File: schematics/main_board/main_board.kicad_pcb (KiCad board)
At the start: 2 copper layers, 184.9 x 184.9 mm, 56 parts, among them J1 USB_B_Micro, M1 Motor_DC, M2 Motor_DC, M3 Motor_DC, M4 Motor_DC, Q1 BC817, Q2 2N7002, Q3 2N7002, Q4 2N7002, Q5 2N7002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

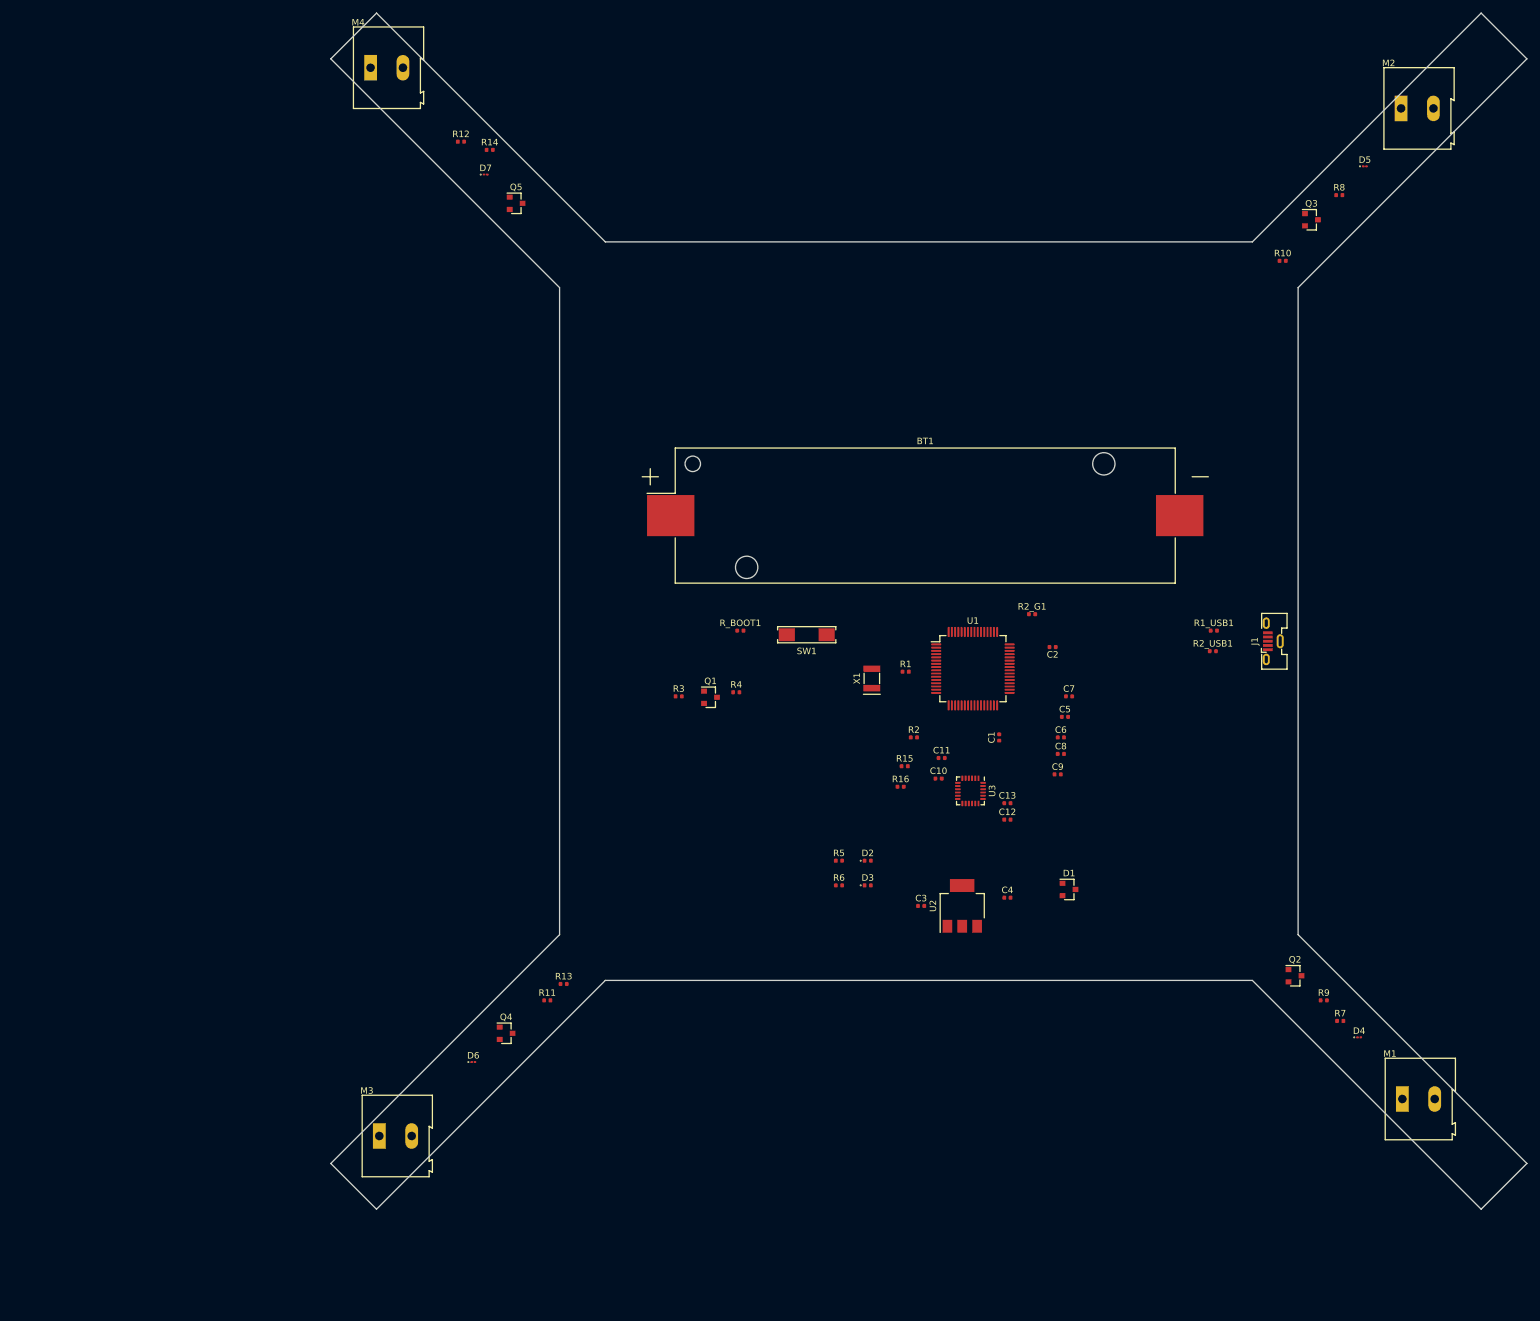
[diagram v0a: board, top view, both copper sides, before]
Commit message: Changed some footprints, added some traces
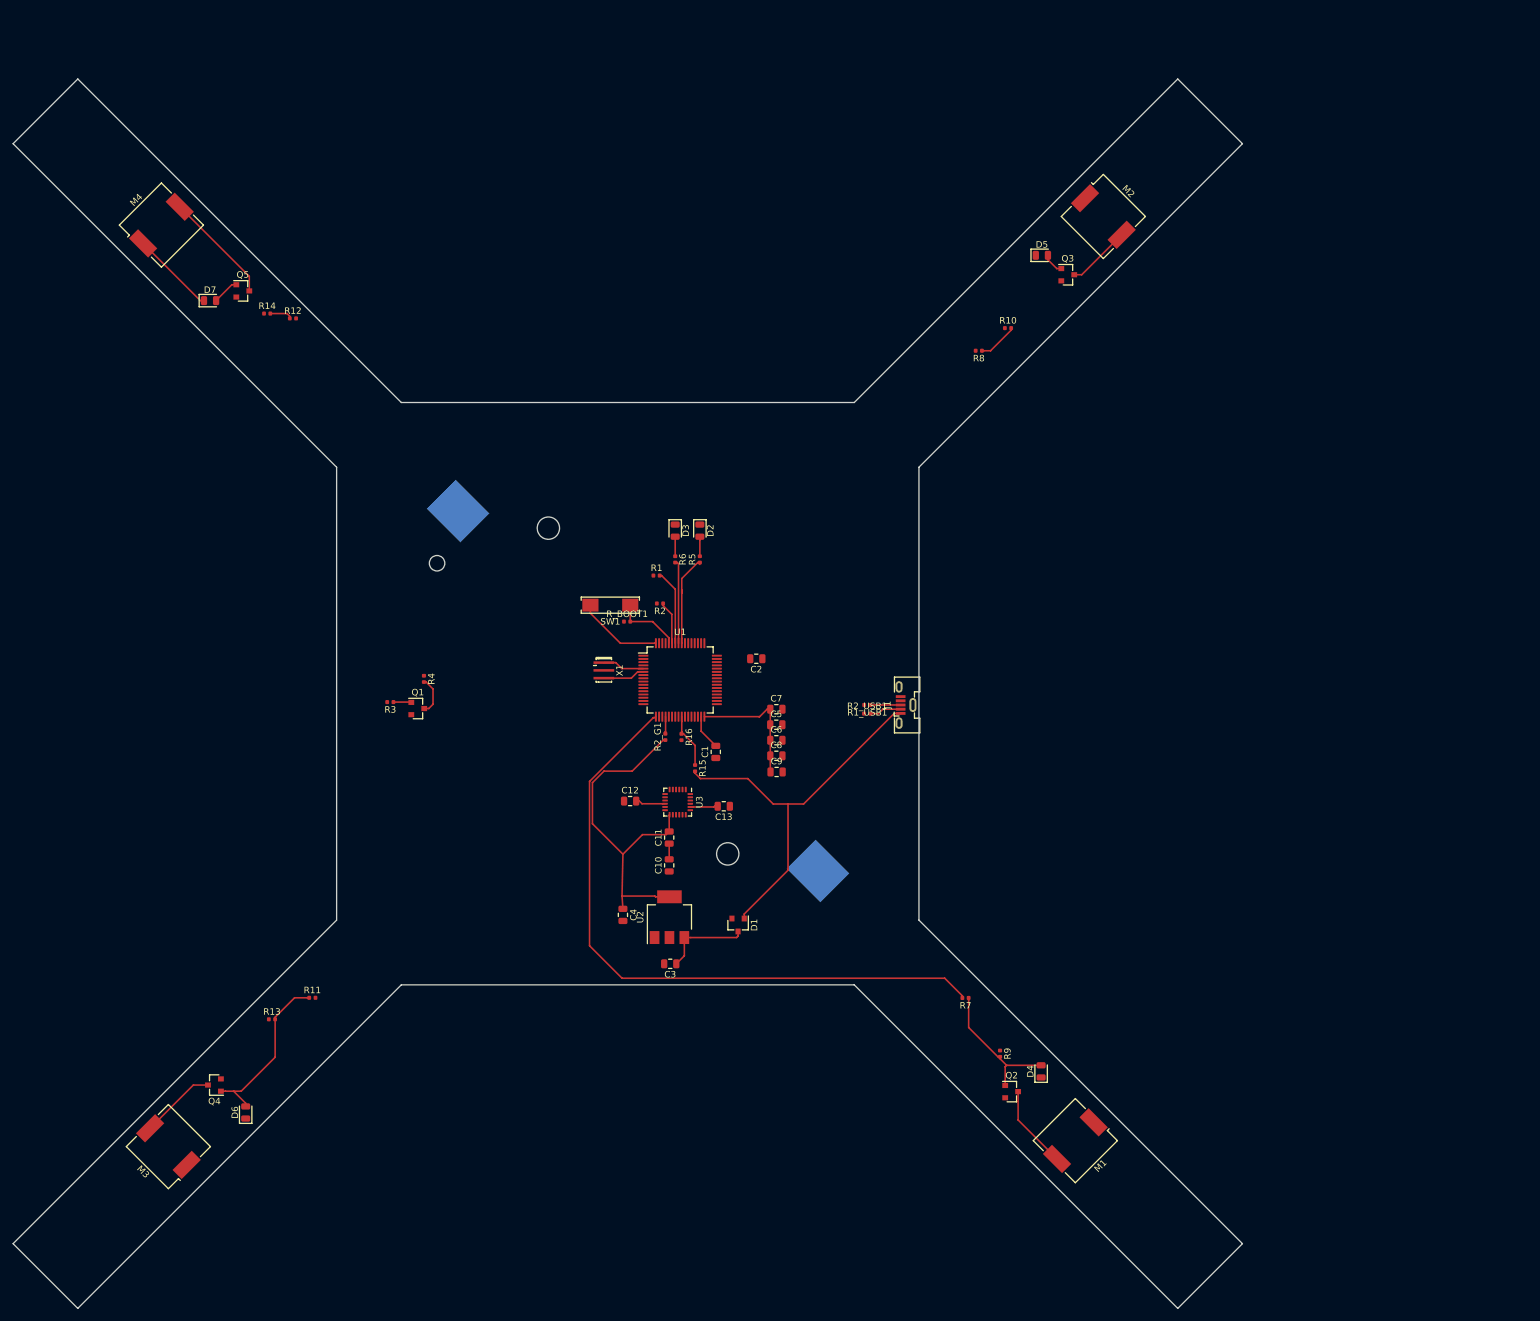
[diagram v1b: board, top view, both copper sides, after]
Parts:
- BT1: moved to B.Cu
- C1, C10, C11, C12, C13, C2, C3, C4, C5, C6, C7, C8, C9: footprint Capacitor_SMD:C_0402_1005Metric -> Capacitor_SMD:C_0805_2012Metric
- D2, D3: footprint LED_SMD:LED_0402_1005Metric -> LED_SMD:LED_0805_2012Metric
- D4, D5, D6, D7: footprint Diode_SMD:D_01005_0402Metric -> Diode_SMD:D_0805_2012Metric
- M1, M2, M3, M4: footprint TerminalBlock:TerminalBlock_Altech_AK300-2_P5.00mm -> Buzzer_Beeper:Buzzer_CUI_CPT-9019S-SMT
- X1: footprint Crystal:Resonator_SMD_muRata_CDSCB-2Pin_4.5x2.0mm -> Crystal:Resonator_SMD_muRata_CSTxExxV-3Pin_3.0x1.1mm_HandSoldering
- moved D3 62.4 mm to (142.3, 119.8), turned to 270 degrees
- moved R8 60.7 mm to (189.2, 92.0), turned to 180 degrees
- moved R2_G1 59.8 mm to (140.8, 151.7), turned to 90 degrees
- moved C4 59.5 mm to (134.2, 179.2), turned to 270 degrees
- moved C12 58.4 mm to (135.4, 161.6)
- moved R7 58.0 mm to (187.2, 192.0), turned to 180 degrees
- moved J1 57.6 mm to (178.0, 146.8)
- moved D2 57.2 mm to (146.1, 119.8), turned to 270 degrees
- moved R6 56.4 mm to (142.3, 124.2), turned to 270 degrees
- moved R1_USB1 54.8 mm to (172.0, 146.7), turned to 180 degrees
- moved R2_USB1 54.3 mm to (172.0, 148.1)
- moved BT1 52.0 mm to (136.6, 144.6), turned to 315 degrees
- moved D5 51.8 mm to (199.0, 77.2)
- moved D1 51.4 mm to (152.1, 180.8), turned to 270 degrees
- moved R5 51.3 mm to (146.1, 124.2), turned to 90 degrees
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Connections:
- BT1 pad 1: VBAT_PAD -> BAT+
- D1 pad 2: 5V_EXTERNAL -> BAT+
- D4 pad 1: VBAT_PAD -> BAT+
- D5 pad 1: VBAT_PAD -> BAT+
- D6 pad 1: VBAT_PAD -> BAT+
- D7 pad 1: VBAT_PAD -> BAT+
- M1 pad 1: VBAT_PAD -> BAT+
- M2 pad 1: VBAT_PAD -> BAT+
- M3 pad 1: VBAT_PAD -> BAT+
- M4 pad 1: VBAT_PAD -> BAT+
- R4 pad 1: 5V_EXTERNAL -> BAT+
- U1 pad 16: M4 -> S4
- U1 pad 17: M1 -> S1
- U1 pad 9: VBAT_PAD -> BAT+
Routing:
- net S1: track 0.00 -> 100.9 mm
- net VCC: track 0.00 -> 87.7 mm
- net 5V_USB: track 0.00 -> 60.3 mm
- net Net-(D6-Pad2): track 0.00 -> 26.4 mm
- net Net-(D4-Pad2): track 0.00 -> 21.6 mm
- net Net-(M4-Pad2): track 0.00 -> 17.5 mm
- net LED1: track 0.00 -> 14.7 mm
- net Net-(C3-Pad1): track 0.00 -> 13.7 mm
- net BAT+: track 0.00 -> 13.1 mm
- net Net-(M1-Pad2): track 0.00 -> 12.9 mm
- net LED2: track 0.00 -> 12.9 mm
- net Net-(M3-Pad2): track 0.00 -> 11.7 mm
- net Net-(R1-Pad2): track 0.00 -> 11.6 mm
- net Net-(R_BOOT1-Pad2): track 0.00 -> 10.4 mm
- net Net-(M2-Pad2): track 0.00 -> 9.88 mm
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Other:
- board size 184.9 x 184.9 mm -> 190 x 190 mm
